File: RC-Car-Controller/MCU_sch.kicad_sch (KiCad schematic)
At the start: 22 parts, among them SW1 SW_Push, SW3 SW_SPDT, U4 STM32H743VGTx, Y1 Crystal

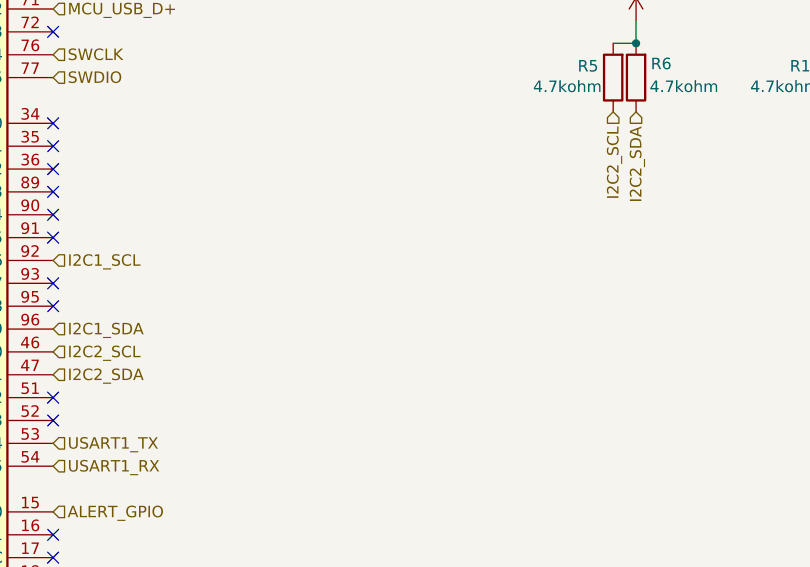
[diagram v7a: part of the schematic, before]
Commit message: Wired up FGH100M
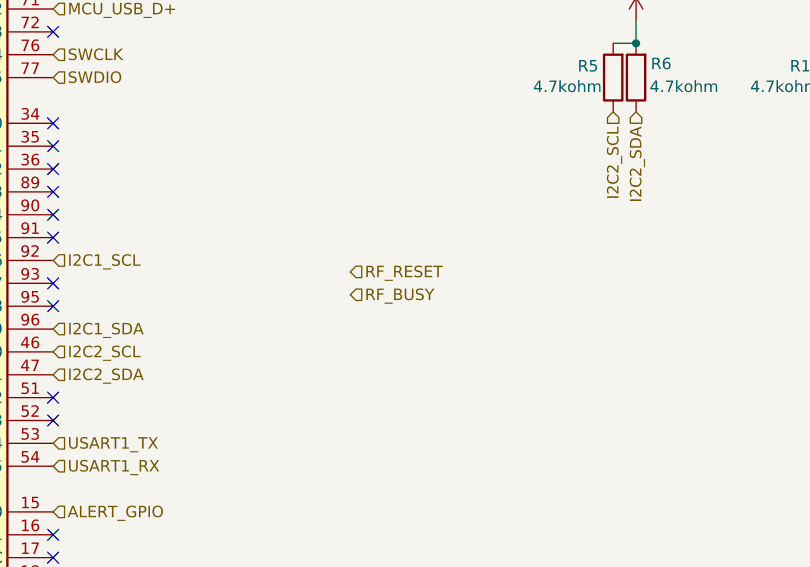
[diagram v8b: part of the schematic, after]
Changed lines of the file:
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@@
+		)
+	)
+	(hierarchical_label "RF_BUSY"
+		(shape input)
+		(at 176.53 105.41 0)
+		(fields_autoplaced yes)
+		(effects
+			(font
+				(size 1.27 1.27)
+			)
+			(justify left)
 		)
 	)
@@
 		(fields_autoplaced yes)
 		(effects
+			(font
+				(size 1.27 1.27)
+			)
+			(justify left)
+		)
+	)
+	(hierarchical_label "RF_RESET"
+		(shape input)
+		(at 176.53 102.87 0)
+		(fields_autoplaced yes)
+		(effects
